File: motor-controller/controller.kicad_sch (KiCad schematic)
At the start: 24 parts

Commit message: Add in some more footprints and components
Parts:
- removed C?: 0.1uF, symbol Device:C_Small
- removed C?: 0.47uF, symbol Device:C_Small
- removed D? (x2): PWR LED, symbol Device:LED
- removed R?: 10k, symbol Device:R_US
- removed R? (x2): 1k, symbol Device:R_US
- removed TP?: TestPoint, symbol Connector:TestPoint
- added C? (x2): 0.1uF, Capacitor_SMD:C_0603_1608Metric_Pad1.08x0.95mm_HandSolder, symbol Device:C_Small
- added C?: 1uF, Capacitor_SMD:C_0805_2012Metric_Pad1.18x1.45mm_HandSolder, symbol Device:C_Small
- added TP?: TestPoint, TestPoint:TestPoint_Pad_D1.0mm, symbol Connector:TestPoint
- C? (x2): value 10uF -> 1uF; footprint (none) -> Capacitor_SMD:C_0805_2012Metric_Pad1.18x1.45mm_HandSolder; Digikey Part Num (none) -> 1276-6470-1-ND
- C?: value 22uF -> 1uF; footprint (none) -> Capacitor_SMD:C_0805_2012Metric_Pad1.18x1.45mm_HandSolder; Digikey Part Num (none) -> 1276-6470-1-ND
- D?: footprint (none) -> LED_SMD:LED_Cree-PLCC4_3.2x2.8mm_CCW
- J?: footprint (none) -> Connector_PinHeader_2.54mm:PinHeader_1x03_P2.54mm_Vertical
- R?: value 8k -> 8.2k; footprint (none) -> Resistor_SMD:R_0603_1608Metric_Pad0.98x0.95mm_HandSolder; Digikey Part Num (none) -> RMCF0603JT8K20CT-ND
- R? (x3): footprint (none) -> Resistor_SMD:R_0603_1608Metric_Pad0.98x0.95mm_HandSolder; Digikey Part Num (none) -> RMCF0603FT470RCT-ND
- R?: footprint (none) -> Resistor_SMD:R_0603_1608Metric_Pad0.98x0.95mm_HandSolder; Digikey Part Num (none) -> RMCF0603FG1K00CT-ND
- TP?: footprint (none) -> TestPoint:TestPoint_Pad_D1.0mm
- U?: value STM32G030F6P6TR -> STM32G030F6P6; Digikey Part Num (none) -> 497-STM32G030F6P6-ND
- U?: Digikey Part Num (none) -> TC1047VNBCT-ND
- U?: Digi-Key_PN NCP1117ST33T3GOSCT-ND -> (none); Digikey Part Num (none) -> NCP1117ST33T3GOSCT-ND
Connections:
- net +3V3: now also C?.1, C?.1
- net +5V: now also U?.3 (OUT)
- net GND: now also U?.2 (GND), C?.2, C?.2, C?.2; no longer U?.1 (ADJ/GND)
- net NRST: now also TP?.1
- net VBUS: now also R?.1, U?.1 (IN), C?.1
- net VBUS_SAMPLE: now also R?.1, R?.2
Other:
- note added: "SWD"
- note removed: "Add Capacitor Here"
- note removed: "Are these decoupling?"
- note removed: "CODE UPLOAD"
- note removed: "DECOUPLING CAPS"
- note removed: "LM2940 HERE"
- note removed: "STM32 MCU"
- note removed: "TODO: Figure out values of decoupling"
- note removed: "TODO: Figure out values of power LEDs"
- note removed: "Use depending on what is desired"
- moved on the sheet: C?, J?, R?

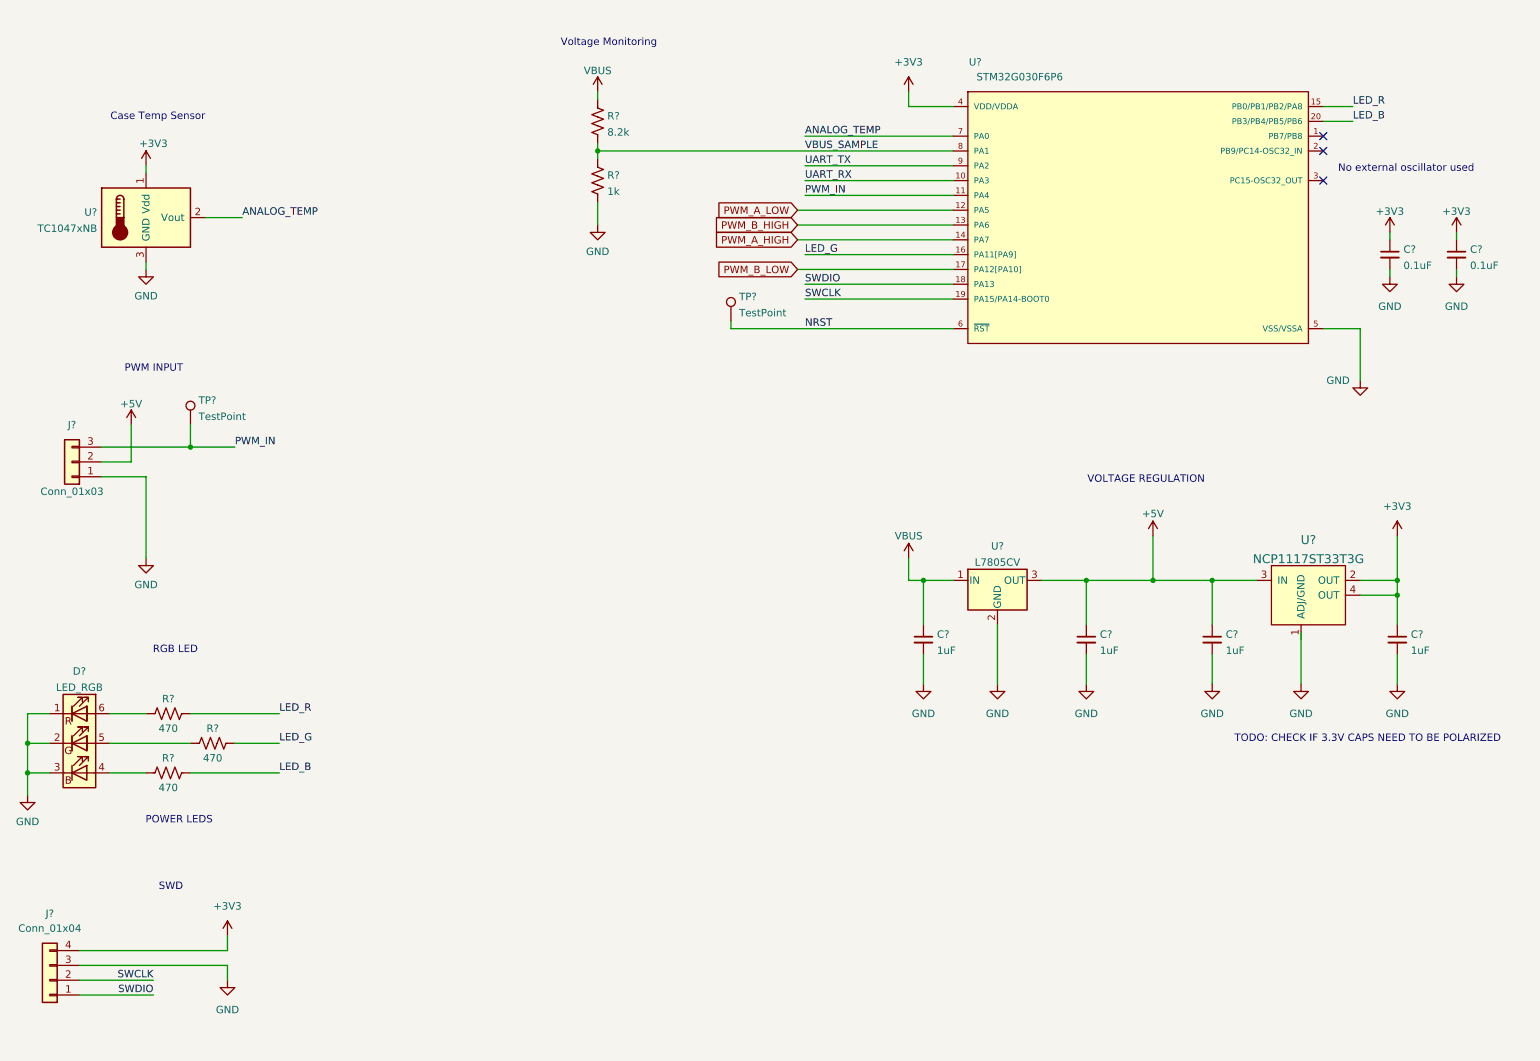
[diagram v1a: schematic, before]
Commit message: Added SEMS footprint
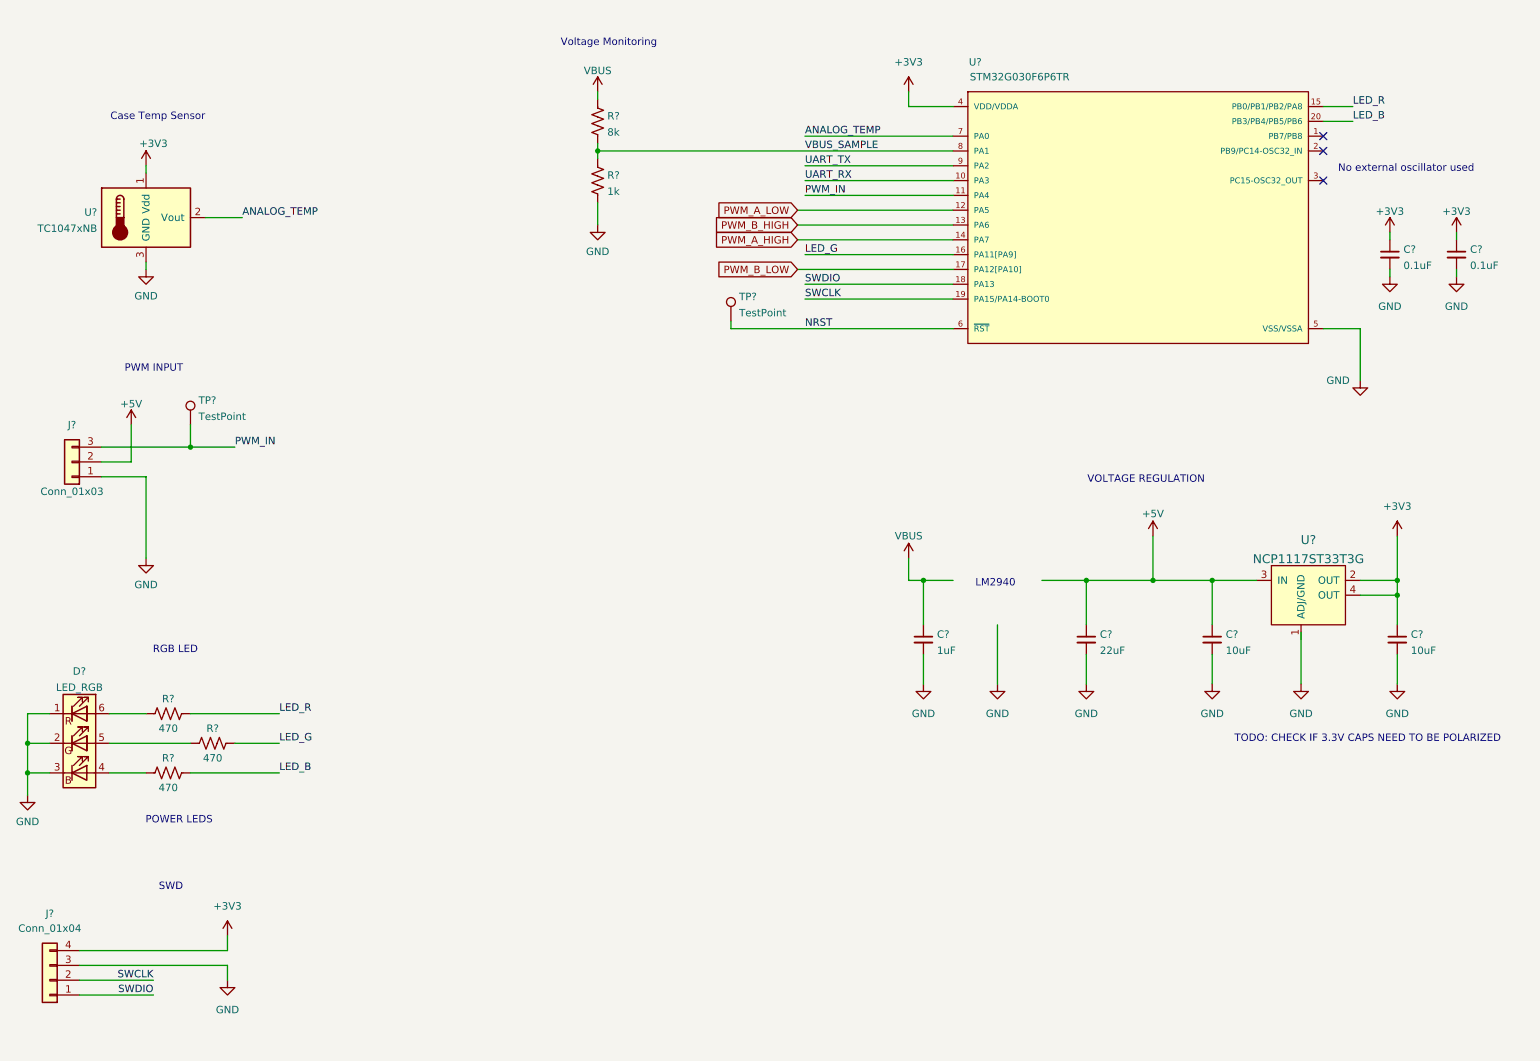
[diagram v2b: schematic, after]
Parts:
- removed U?: L7805CV, symbol Regulator_Linear:L7805
- C? (x2): value 1uF -> 10uF
- C?: value 1uF -> 22uF
- R?: value 8.2k -> 8k
- U?: value STM32G030F6P6 -> STM32G030F6P6TR
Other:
- note added: "LM2940"

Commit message: first stab at placement
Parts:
- removed D?: LED_RGB, LED_SMD:LED_Cree-PLCC4_3.2x2.8mm_CCW, symbol Device:LED_RGB
- removed J?: Conn_01x04, Connector:FanPinHeader_1x04_P2.54mm_Vertical, symbol Connector_Generic:Conn_01x04
- removed TP? (x2): TestPoint, TestPoint:TestPoint_Pad_D1.0mm, symbol Connector:TestPoint
- added C4: 0.1uF, Capacitor_SMD:C_0603_1608Metric_Pad1.08x0.95mm_HandSolder, symbol Device:C_Small
- added D3: CLV1A-FKB, LED_SMD:LED_Cree-PLCC4_3.2x2.8mm_CCW, symbol Device:LED_RABG
- added J5: Conn_01x05, Connector_PinHeader_2.54mm:PinHeader_1x05_P2.54mm_Vertical, symbol Connector_Generic:Conn_01x05
- added R14: 0, Resistor_SMD:R_0603_1608Metric_Pad0.98x0.95mm_HandSolder, symbol Device:R_US
- added U6: LM78M05, Package_TO_SOT_SMD:TO-252-2, symbol Regulator_Linear:LM78M05_TO252
- U4: renamed from U?; footprint STMicroelectronics-TSSOP20-YA-0-3-* -> Package_SO:SSOP-20_4.4x6.5mm_P0.65mm
- U5: renamed from U?; footprint digikey-footprints:SOT-223 -> Package_TO_SOT_SMD:SOT-223
- gave numbers to parts that had none: 13
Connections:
- net +3V3: now also C4.1, J5.1 (Pin_1), R14.1
- net +5V: now also U6.3 (VO)
- net GND: now also C4.2, J5.2 (Pin_2), U6.2 (GND)
- net NRST: now also J5.5 (Pin_5)
- net SWCLK: now also J5.3 (Pin_3)
- net SWDIO: now also J5.4 (Pin_4)
- net VBUS: now also U6.1 (VI)
- net at R11.1: now also D3.4 (GK)
- net at R9.1: now also D3.1 (RK)
- net at R10.1: now also D3.3 (BK)
- new net: D3.2 (A), R14.2
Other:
- note removed: "LM2940"
- note removed: "POWER LEDS"
- moved on the sheet: R10, R11, R9
